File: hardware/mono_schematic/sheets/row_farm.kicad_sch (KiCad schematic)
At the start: 98 parts

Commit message: mono_electronics v11b: TLV75733P 1A AON LDO, 22uF ESP32 bulk, LED_EN RC glitch filter, J_USB value, refs end in digit; schematic regenerated (ERC 0, 0 diffs)
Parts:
- removed J_ROW: FFC_40P_050_ROW, mono_electronics:FFC_40P_050_ROW, symbol mono_parts:FFC_40P_050_ROW_FFC_40P_050_ROW_40
- removed R_GN: 2.2k, mono_electronics:R_0402_1005Metric, symbol mono_parts:2.2k_R_0402_1005Metric_2
- added J_ROW1: FFC_40P_050_ROW, mono_electronics:FFC_40P_050_ROW, symbol mono_parts:FFC_40P_050_ROW_FFC_40P_050_ROW_40
- added R_GN1: 2.2k, mono_electronics:R_0402_1005Metric, symbol mono_parts:2.2k_R_0402_1005Metric_2
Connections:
- net AUD_FB: now also R_GN1.1
- net AUD_GC: now also R_GN1.2
- net ROW_01_ANODE: now also J_ROW1.1 (ROW_01_ANODE)
- net ROW_02_ANODE: now also J_ROW1.2 (ROW_02_ANODE)
- net ROW_03_ANODE: now also J_ROW1.3 (ROW_03_ANODE)
- net ROW_04_ANODE: now also J_ROW1.4 (ROW_04_ANODE)
- net ROW_05_ANODE: now also J_ROW1.5 (ROW_05_ANODE)
- net ROW_06_ANODE: now also J_ROW1.6 (ROW_06_ANODE)
- net ROW_07_ANODE: now also J_ROW1.7 (ROW_07_ANODE)
- net ROW_08_ANODE: now also J_ROW1.8 (ROW_08_ANODE)
- net ROW_09_ANODE: now also J_ROW1.9 (ROW_09_ANODE)
- net ROW_10_ANODE: now also J_ROW1.10 (ROW_10_ANODE)
- net ROW_11_ANODE: now also J_ROW1.11 (ROW_11_ANODE)
- net ROW_12_ANODE: now also J_ROW1.12 (ROW_12_ANODE)
- net ROW_13_ANODE: now also J_ROW1.13 (ROW_13_ANODE)
- net ROW_14_ANODE: now also J_ROW1.14 (ROW_14_ANODE)
- net ROW_15_ANODE: now also J_ROW1.15 (ROW_15_ANODE)
- net ROW_16_ANODE: now also J_ROW1.16 (ROW_16_ANODE)
- net ROW_17_ANODE: now also J_ROW1.17 (ROW_17_ANODE)
- net ROW_18_ANODE: now also J_ROW1.18 (ROW_18_ANODE)
- net ROW_19_ANODE: now also J_ROW1.19 (ROW_19_ANODE)
- net ROW_20_ANODE: now also J_ROW1.20 (ROW_20_ANODE)
- net ROW_21_ANODE: now also J_ROW1.21 (ROW_21_ANODE)
- net ROW_22_ANODE: now also J_ROW1.22 (ROW_22_ANODE)
- net ROW_23_ANODE: now also J_ROW1.23 (ROW_23_ANODE)
- net ROW_24_ANODE: now also J_ROW1.24 (ROW_24_ANODE)
- net ROW_25_ANODE: now also J_ROW1.25 (ROW_25_ANODE)
- net ROW_26_ANODE: now also J_ROW1.26 (ROW_26_ANODE)
- net ROW_27_ANODE: now also J_ROW1.27 (ROW_27_ANODE)
- net ROW_28_ANODE: now also J_ROW1.28 (ROW_28_ANODE)
- net ROW_29_ANODE: now also J_ROW1.29 (ROW_29_ANODE)
- net ROW_30_ANODE: now also J_ROW1.30 (ROW_30_ANODE)
- net ROW_31_ANODE: now also J_ROW1.31 (ROW_31_ANODE)
- net ROW_32_ANODE: now also J_ROW1.32 (ROW_32_ANODE)

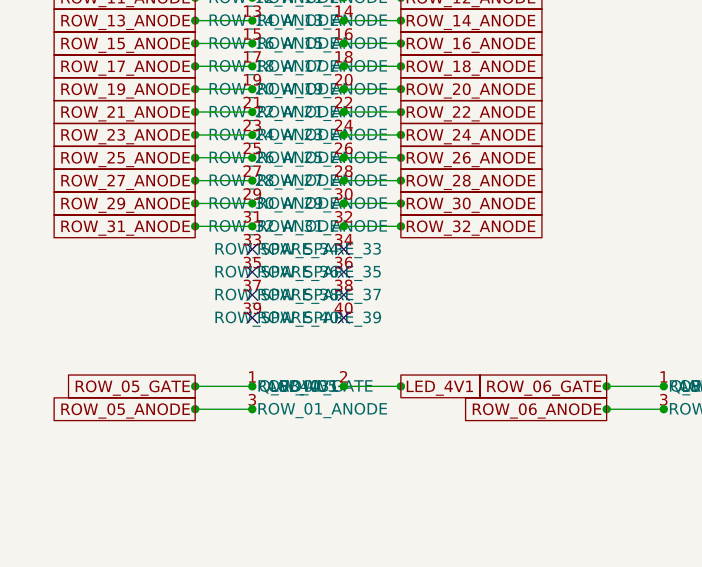
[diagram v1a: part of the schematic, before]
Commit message: mono_electronics v12: LED interface standard on FFC spares (ID I2C 33R+PESD5V0S2BT, ID_3V3 100R, GND 33/38/40; DNP column-expansion taps incl. U_LED2 SDO), schematic regen (ERC 0, 0 diffs), fab v12; garland 480 Hz scan mode (scan_div) + timing fix
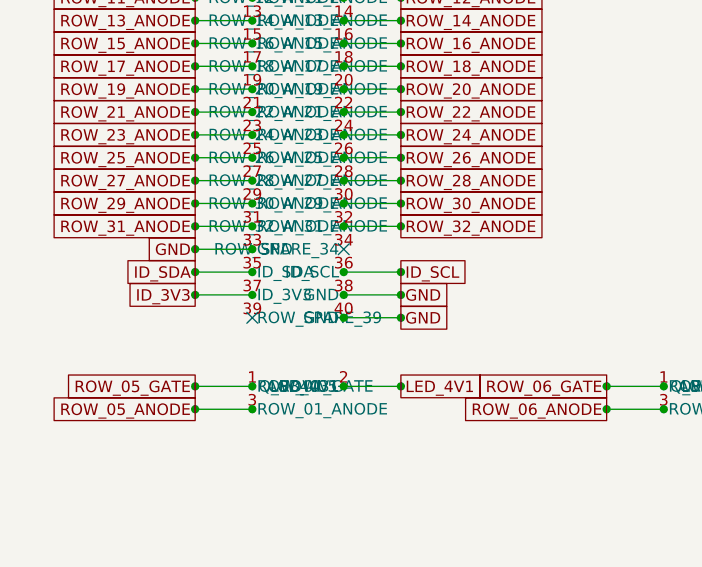
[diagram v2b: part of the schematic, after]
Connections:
- net GND: now reaches J_ROW1.33 (GND)
- net GND: now also J_ROW1.38 (GND), J_ROW1.40 (GND)
- net ID_SDA: now reaches J_ROW1.35 (ID_SDA)
- net ID_SCL: now reaches J_ROW1.36 (ID_SCL)
- net ID_3V3: now reaches J_ROW1.37 (ID_3V3)
- no-connect marks 8 -> 2
